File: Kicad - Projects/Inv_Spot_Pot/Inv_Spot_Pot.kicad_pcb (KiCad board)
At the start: 2 copper layers, 189.9 x 126.8 mm, 72 parts, among them J1 Screw_Terminal_01x03, J2 PWM, J3 Display_Power, J4 Current_Sense, J5 PWM, Q1 40T120, Q2 40T120, Q3 40T120, Q4 40T120, T1 Transformer_1P_2S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

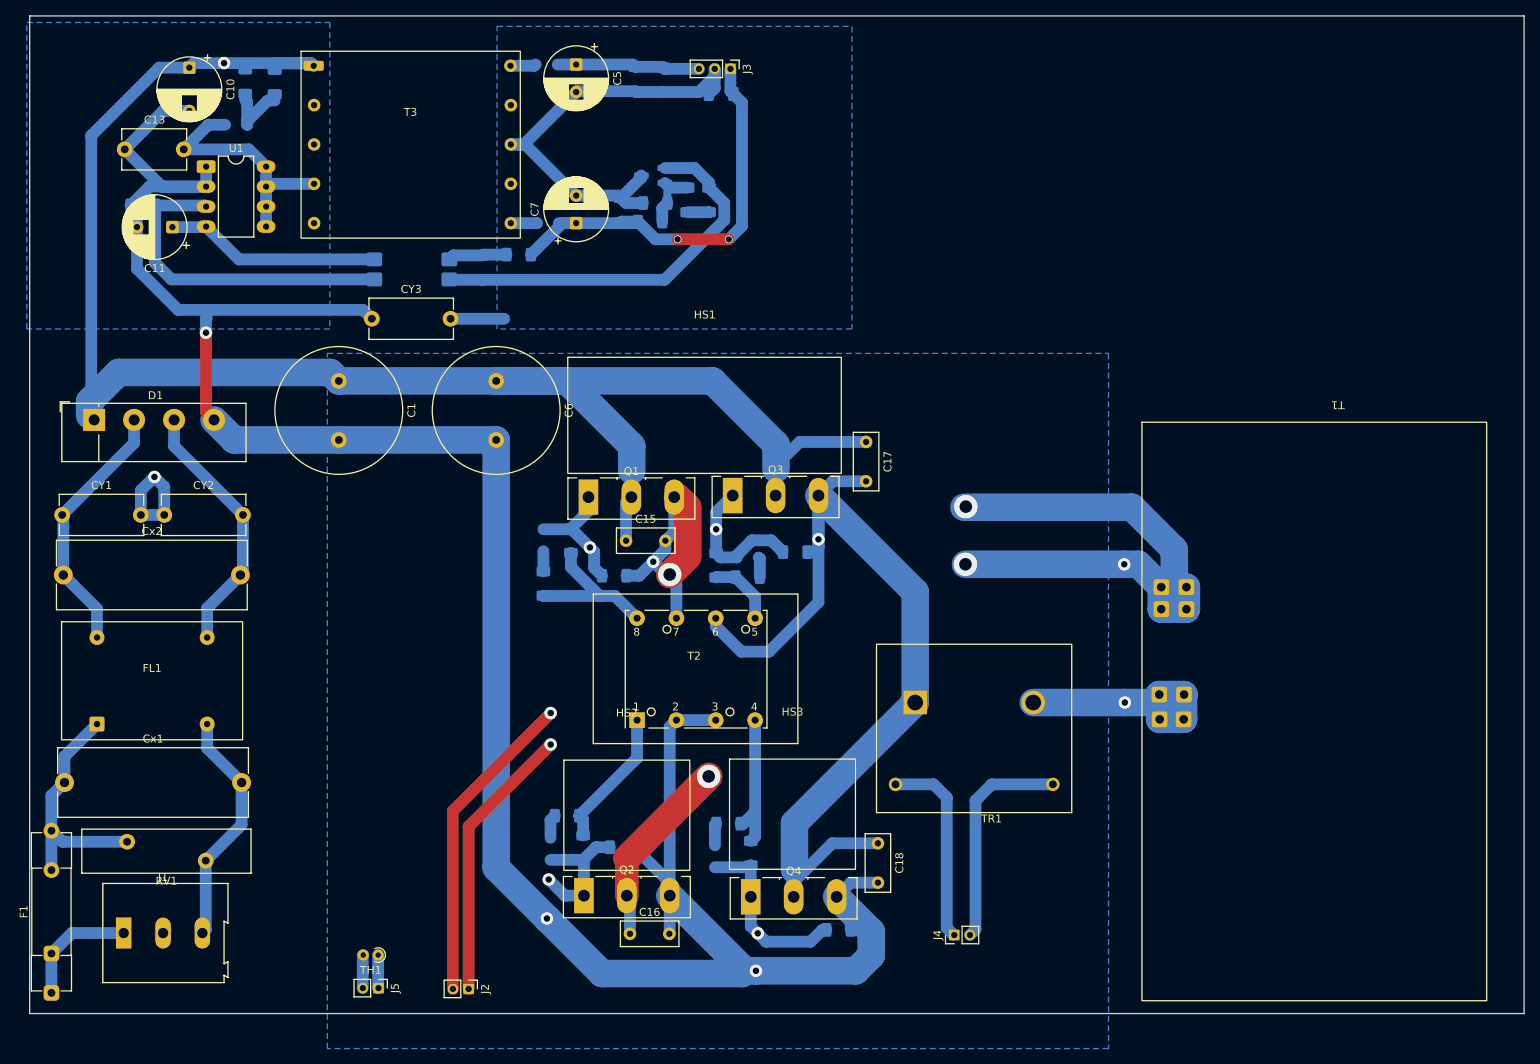
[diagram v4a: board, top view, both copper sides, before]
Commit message: Ajustes Finais
Ajustes em larguras de trilha da camada top

Ajuste do footprint dos capacitores de polipropileno dos IGBTs

Ajuste dos planos de referência
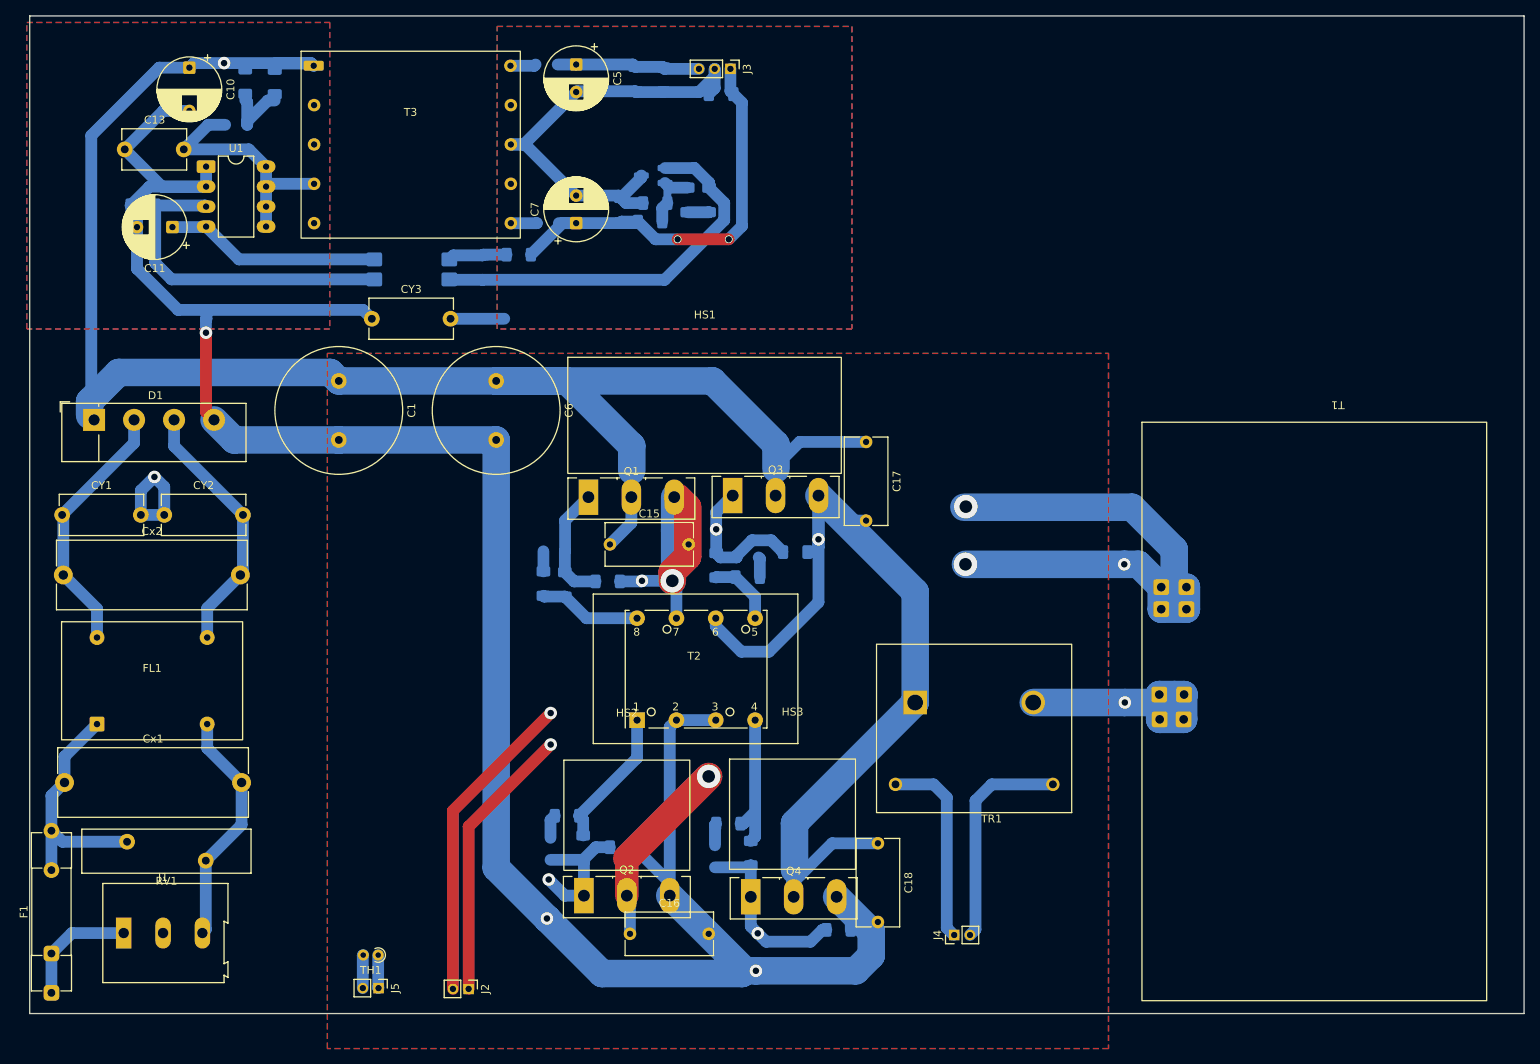
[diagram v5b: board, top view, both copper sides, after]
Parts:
- C15, C16, C17, C18: footprint Capacitor_THT:C_Rect_L7.2mm_W3.0mm_P5.00mm_FKS2_FKP2_MKS2_MKP2 -> Capacitor_THT:C_Rect_L11.0mm_W5.3mm_P10.00mm_MKT
- moved R6 5.60 mm to (101.2, 102.2)
- moved C15 2.10 mm to (106.9, 97.2)
- moved D5 1.94 mm to (99.8, 98.0), turned to 0 degrees
- moved R3 1.10 mm to (106.6, 101.9)
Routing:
- net PWM: track 20.1 -> 13.1 mm
- net Earth: track 310.7 -> 306.4 mm
- net T-: track 133.4 -> 137.2 mm
- net 310V: track 217.1 -> 218.4 mm
- net Gate: track 16.1 -> 15.2 mm, vias 1 -> 0
- net T+: track 122.9 -> 123.4 mm
- added copper zone on F.Cu, net Earth
- added copper zone on F.Cu, net GND

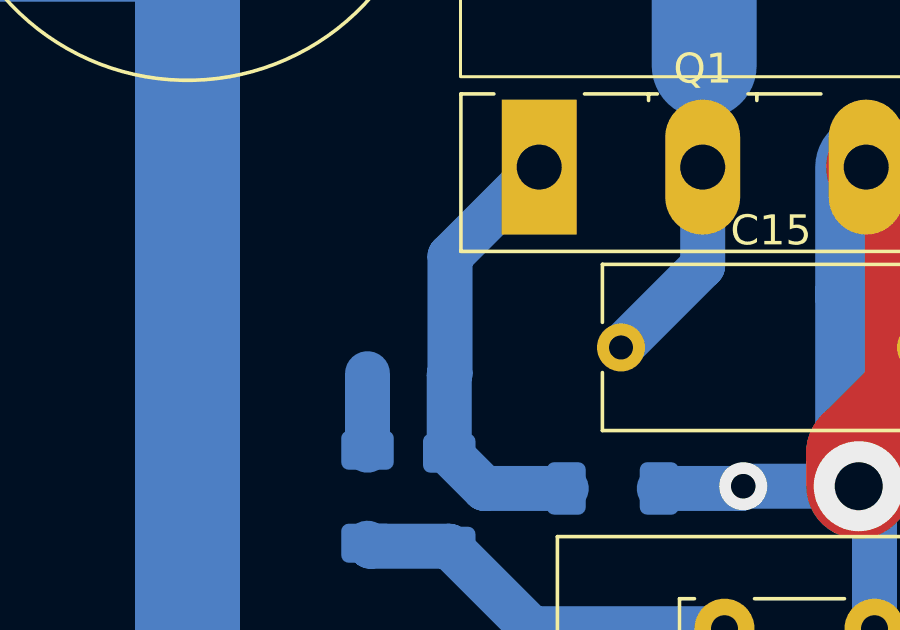
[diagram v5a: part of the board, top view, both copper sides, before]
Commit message: Ponto de Teste Restaurado
Alteração prévia acidentalmente removeu ponto de teste no gate (Q1), adicionado novamente
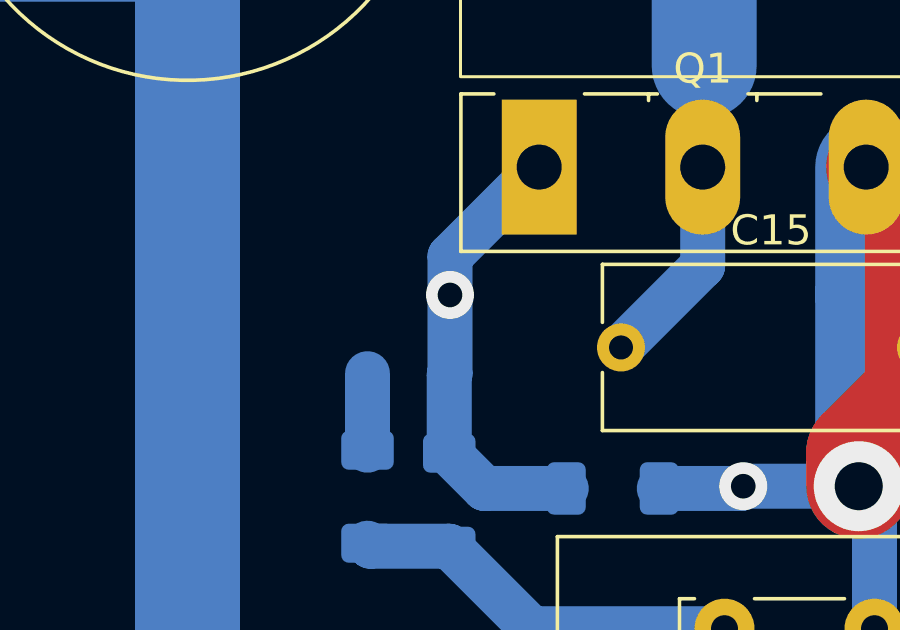
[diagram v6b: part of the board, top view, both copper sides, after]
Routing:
- net Gate: vias 0 -> 1
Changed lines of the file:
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@@
 		(net "Gate1")
+	)
+	(via
+		(at 101.2 95.425)
+		(size 1.6)
+		(drill 0.82)
+		(layers "F.Cu" "B.Cu")
+		(net "Gate")
 	)
 	(segment
@@
 		(start 101.175 100.7)
 		(end 101.175 98.075)
+		(width 1.5)
+		(layer "B.Cu")
+		(net "Gate")
+	)
+	(segment
+		(start 101.2 95.425)
+		(end 101.2 94.136038)
 		(width 1.5)
 		(layer "B.Cu")
@@
 	(segment
 		(start 101.2 98.05)
-		(end 101.2 94.136038)
+		(end 101.2 95.425)
 		(width 1.5)
 		(layer "B.Cu")

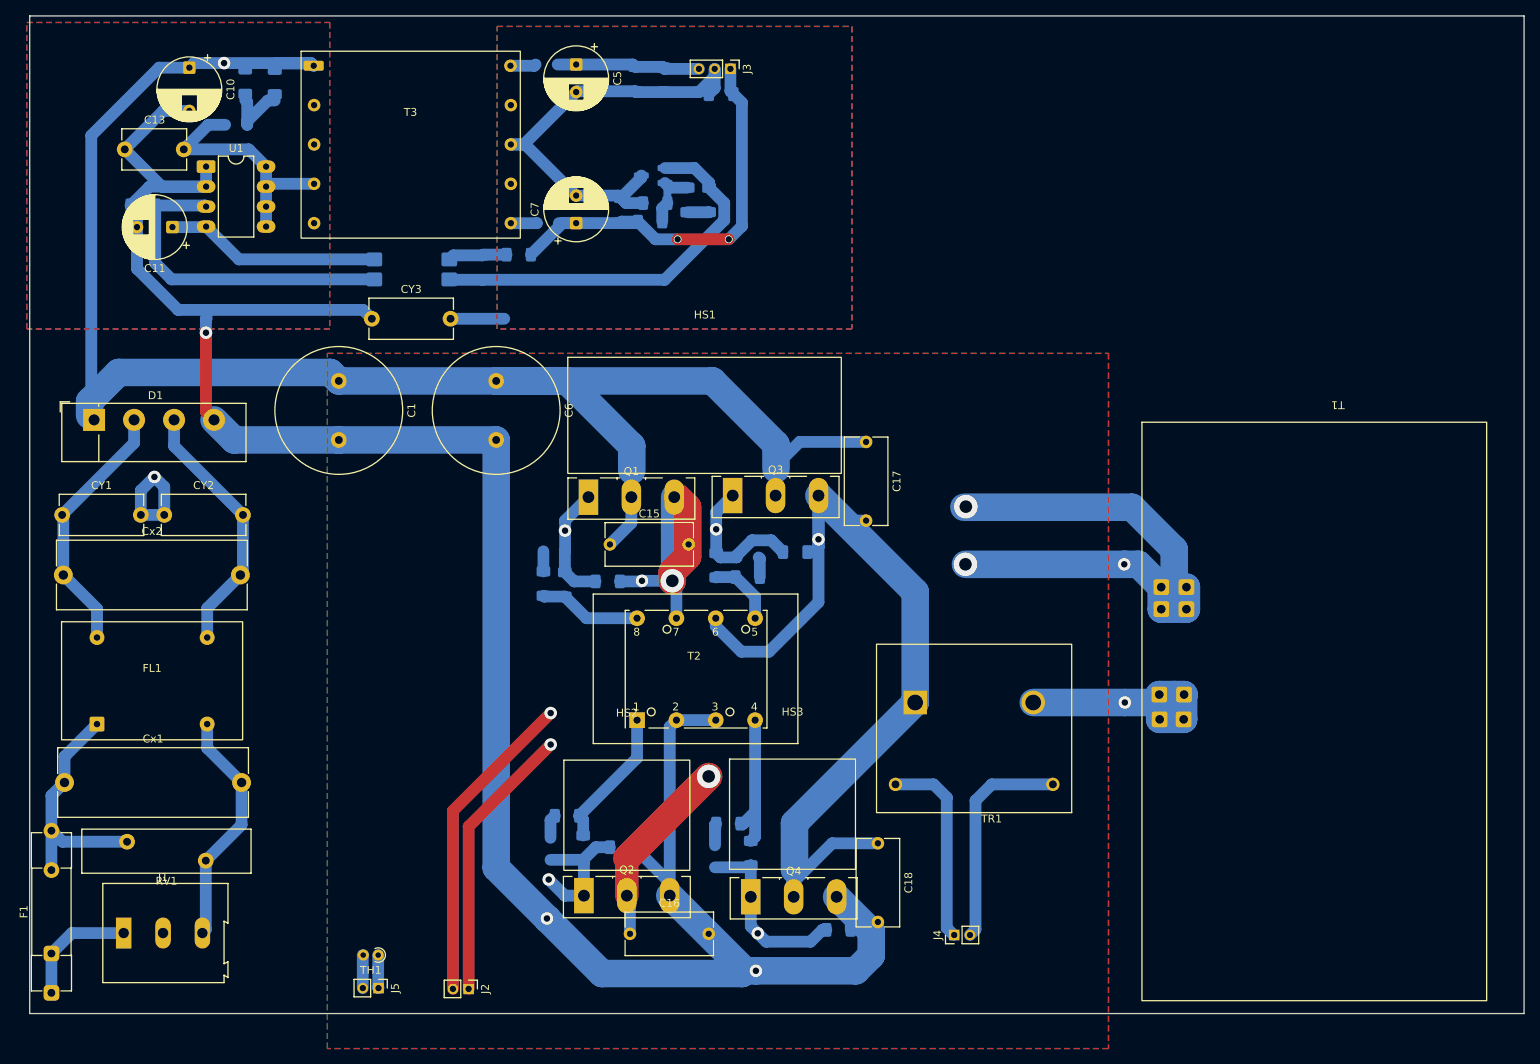
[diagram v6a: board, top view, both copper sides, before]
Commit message: Ajustes de Footprint
Ajustadas footprints para valores disponíveis

Falta:
 - Adicionar GND e 5V nos pinos de programação do display
 - Adicionar resistor de 5V para Temp_Sense, possibilitando leitura de temperatura
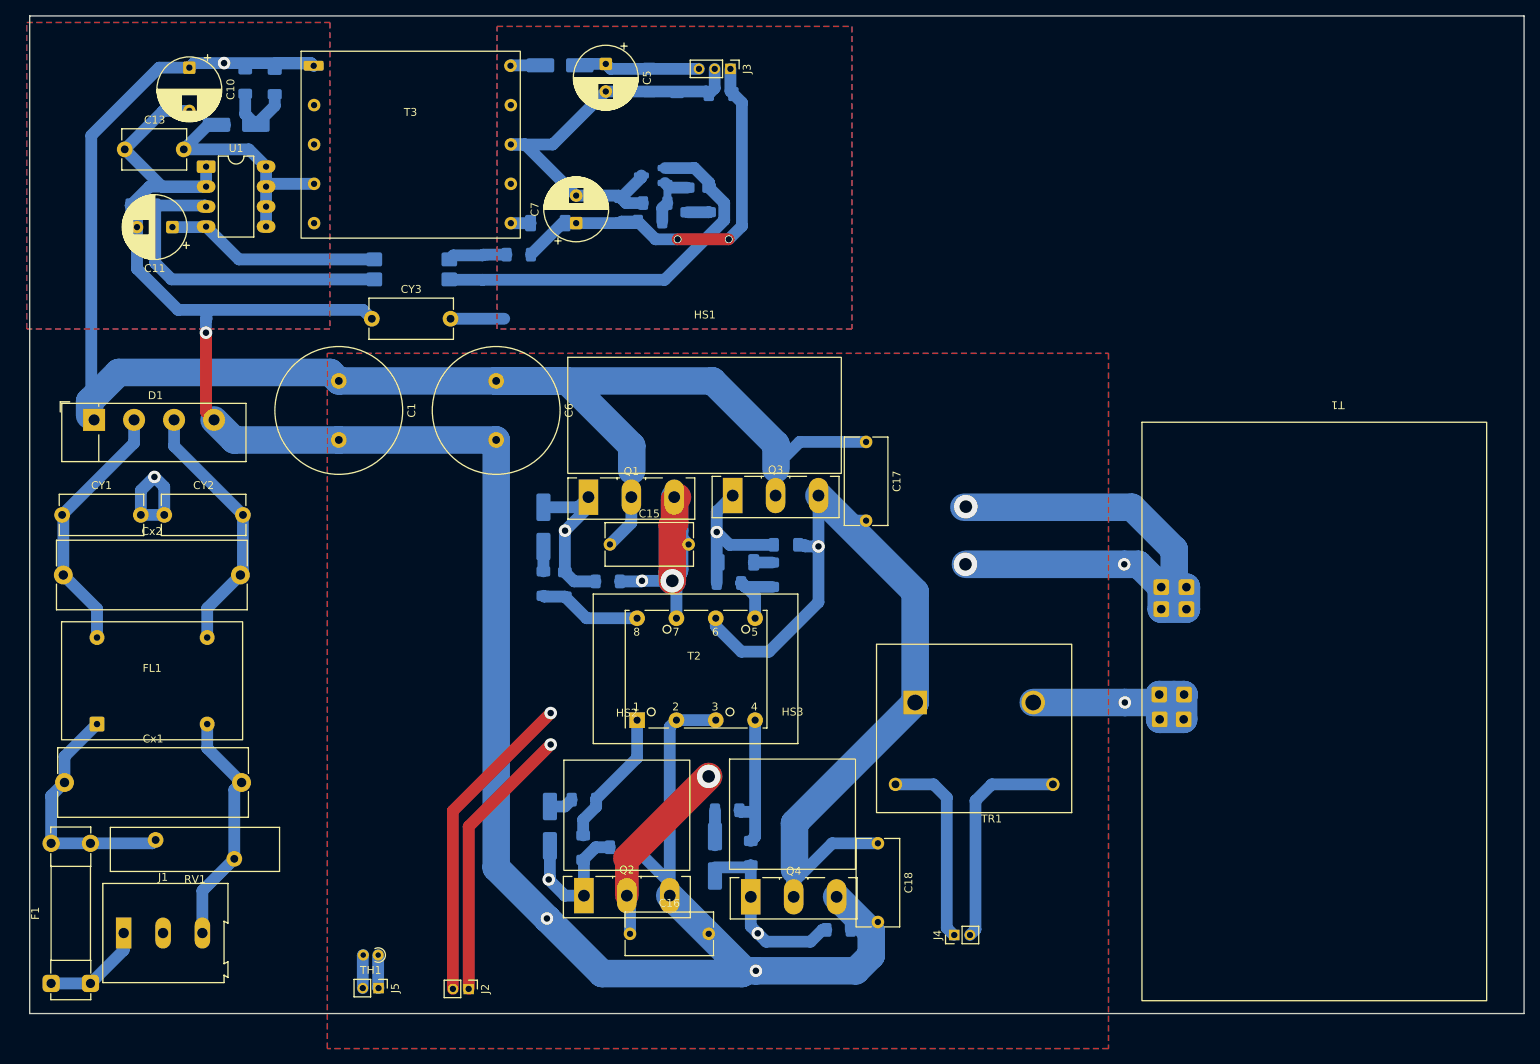
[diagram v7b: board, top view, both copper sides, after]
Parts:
- D2: footprint Diode_SMD:D_SOD-123F -> Diode_SMD:D_SMA_Handsoldering
- D3, D4, D5, D8: value K7 -> SS16; footprint Diode_SMD:D_SOD-123F -> Diode_SMD:D_SMA_Handsoldering
- D6, D7: value K7 -> SS16; footprint Diode_SMD:D_SOD-123F -> Diode_SMD:D_SOD-128
- F1: footprint Fuse:Fuseholder_Clip-5x20mm_Schurter_CQM_Inline_P20.60x5.00mm_D1.00mm_Horizontal -> Fuse:Fuseholder_Clip-5x20mm_Bel_FC-203-22_Lateral_P17.80x5.00mm_D1.17mm_Horizontal
- moved C5 3.76 mm to (106.4, 36.1)
- moved RV1 3.63 mm to (49.2, 134.7)
- moved D5 3.38 mm to (98.5, 95.0), turned to 90 degrees
- moved R17 3.14 mm to (127.5, 101.0), turned to -90 degrees
- moved R1 2.97 mm to (103.6, 129.6)
- moved D3 2.88 mm to (99.3, 133.0)
- moved R18 2.78 mm to (122.0, 102.1), turned to 0 degrees
- moved R14 1.78 mm to (111.9, 38.2)
- moved C8 1.78 mm to (115.4, 38.2)
- moved D4 1.72 mm to (100.6, 36.3)
- moved R19 1.71 mm to (121.8, 130.9)
- moved D7 1.56 mm to (123.0, 99.5)
- moved R13 1.50 mm to (129.3, 97.2)
- moved F1 1.20 mm to (35.9, 152.9)
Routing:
- net Gate: track 15.2 -> 21.4 mm
- net T+: track 123.4 -> 117.9 mm
- net 5V: track 18.2 -> 15.5 mm
- net GND: track 64.7 -> 62.2 mm
- net Net-(J1-Pin_1): track 14.9 -> 13.1 mm
- net Net-(D8-K): track 2.81 -> 4.45 mm
- net Gate1: track 18.5 -> 19.8 mm
- net T-: track 137.2 -> 136.1 mm
- net 15V: track 55.2 -> 54.4 mm
- net Net-(D6-A): track 3.30 -> 2.50 mm
- net PWM1: track 8.73 -> 9.44 mm
- net Net-(D5-K): track 2.55 -> 3.15 mm
- net Net-(D4-A): track 3.27 -> 3.84 mm
- net Net-(D2-K): track 8.29 -> 7.78 mm

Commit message: Ajustes Gerais
Ajustes Gerais
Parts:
- moved C11 2.82 mm to (51.5, 59.6)
- moved C12 2.82 mm to (48.2, 56.9)
- moved U1 2.47 mm to (55.7, 51.6)
- moved C10 2.17 mm to (51.3, 37.2)
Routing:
- net 310V: track 218.4 -> 179.1 mm
- net Earth: track 306.4 -> 286.2 mm
- net Net-(U1-FB): track 42.5 -> 40.2 mm
- net Net-(D2-A): track 31.8 -> 32.8 mm
